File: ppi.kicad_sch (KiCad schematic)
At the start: 6 parts

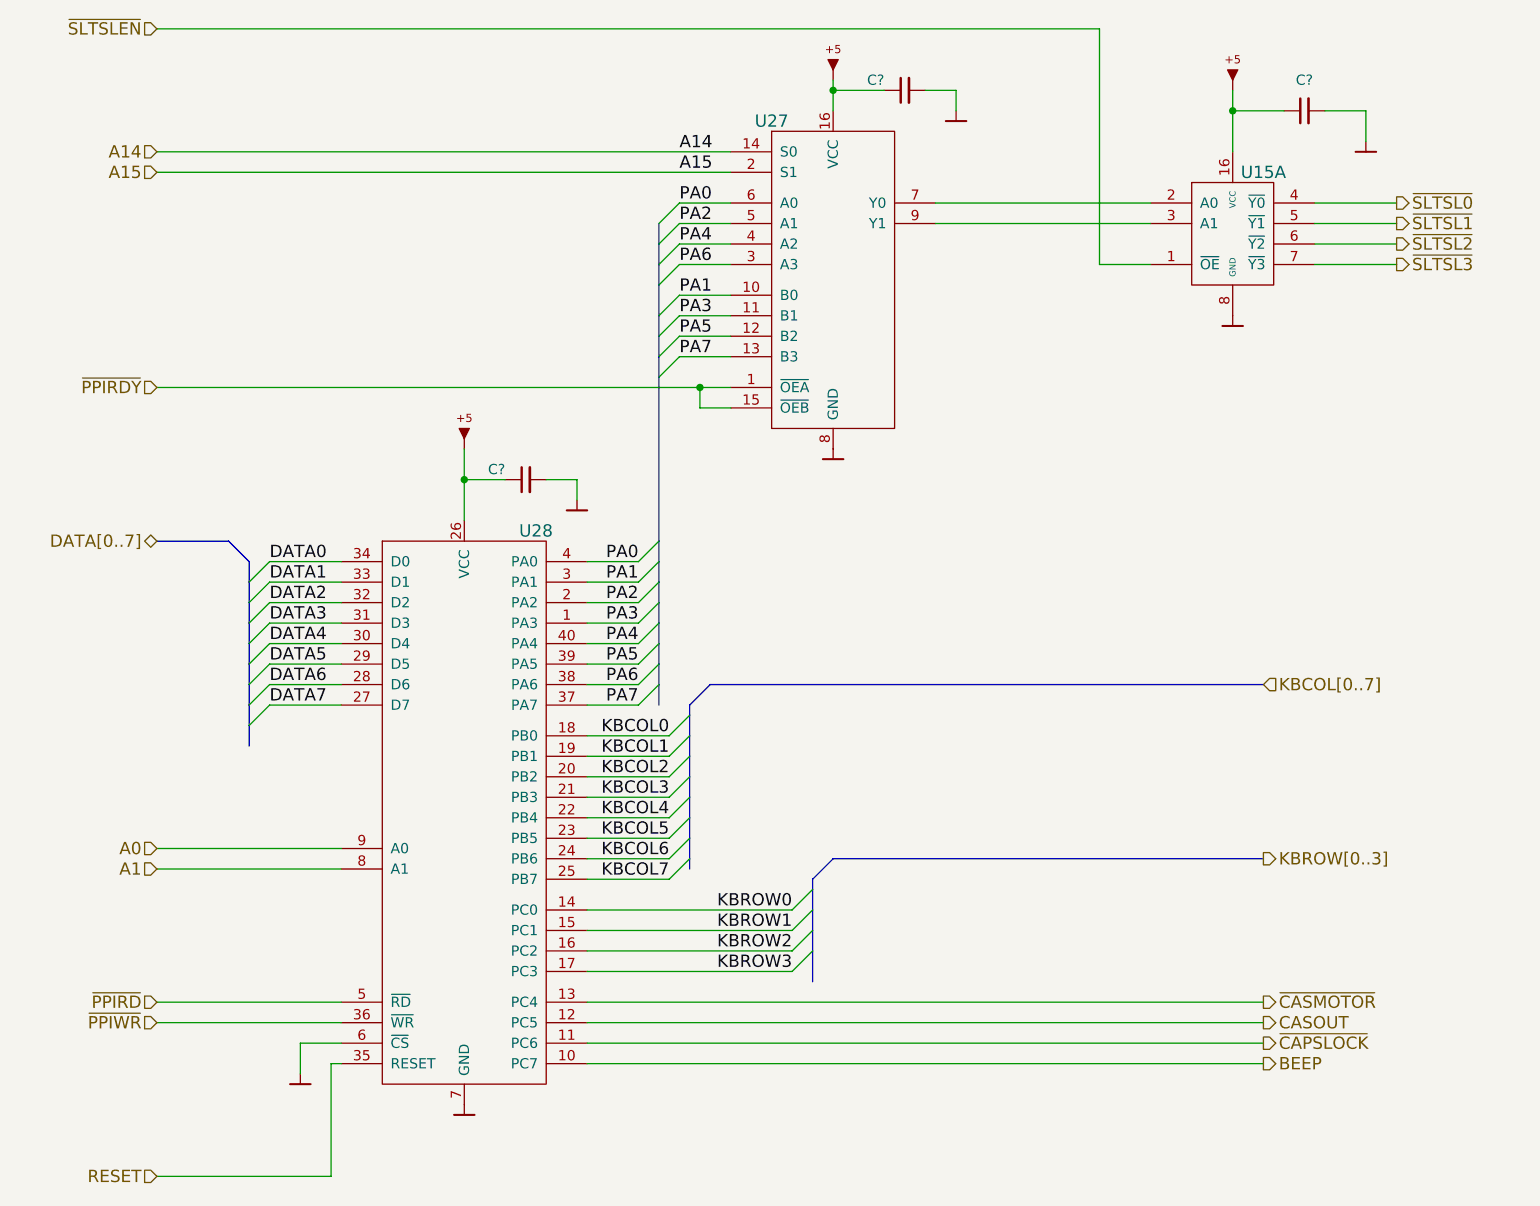
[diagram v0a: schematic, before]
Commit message: Implement power transform circuit
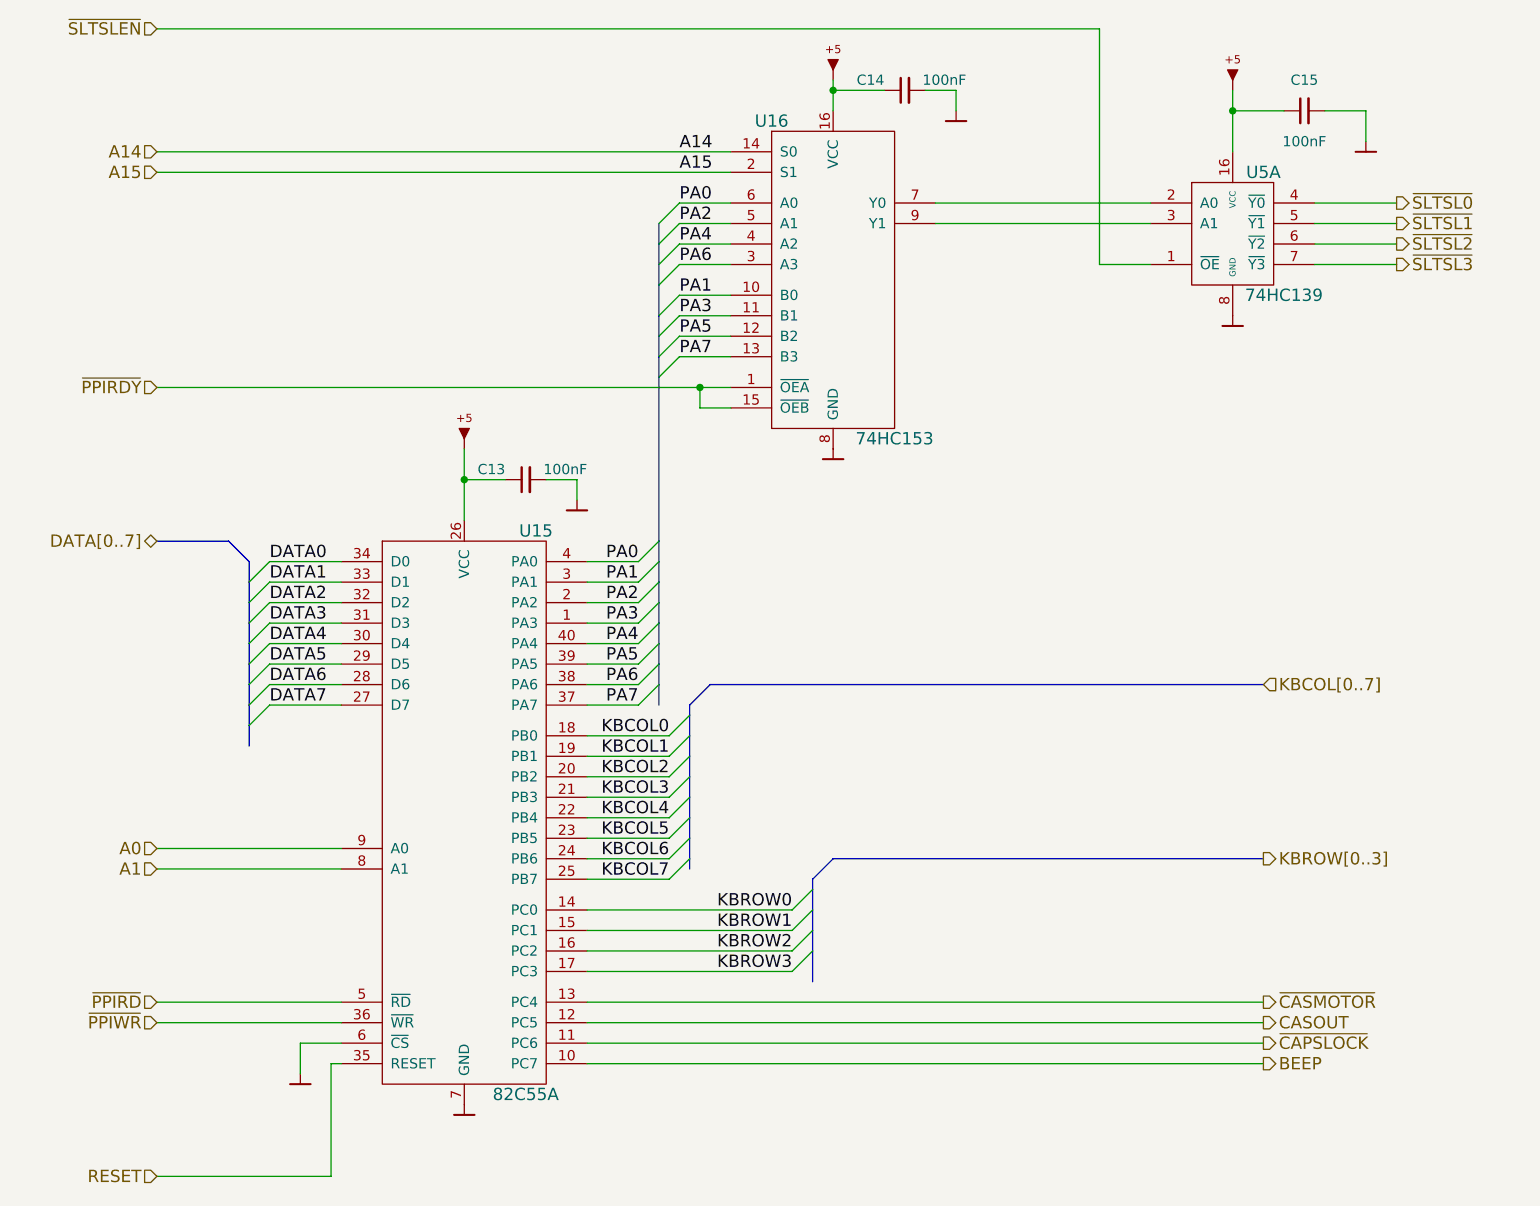
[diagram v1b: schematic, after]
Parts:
- C13, C14, C15: renamed from C?; value (none) -> 100nF; footprint (none) -> artemisa:Disc_capacitor
- U15: renamed from U28; value (none) -> 82C55A; footprint (none) -> artemisa:DIP-40_600
- U16: renamed from U27; value (none) -> 74HC153; footprint (none) -> artemisa:DIP-16_300
- U5: renamed from U15; value (none) -> 74HC139; footprint (none) -> artemisa:DIP-16_300
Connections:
- net VCC: now reaches C13.1, U15.26 (VCC)
- net VCC: now also C14.1, C15.1, U16.16 (VCC), U5.16 (VCC)
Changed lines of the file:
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@@
   (symbol (lib_id "artemisa:82C55A") (at 114.3 127 0) (unit 1)
     (in_bom yes) (on_board yes)
-    (property "Reference" "U28" (id 0) (at 123.19 90.17 0)
-      (effects (font (size 1.524 1.524)))
-    )
-    (property "Value" "" (id 1) (at 121.92 160.02 0)
-      (effects (font (size 1.524 1.524)))
-    )
-    (property "Footprint" "" (id 2) (at 119.38 113.03 0)
+    (property "Reference" "U15" (id 0) (at 123.19 90.17 0)
+      (effects (font (size 1.524 1.524)))
+    )
+    (property "Value" "82C55A" (id 1) (at 121.92 160.02 0)
+      (effects (font (size 1.524 1.524)))
+    )
+    (property "Footprint" "artemisa:DIP-40_600" (id 2) (at 119.38 113.03 0)
       (effects (font (size 1.524 1.524)) hide)
     )
@@
   (symbol (lib_id "artemisa:74HC153") (at 160.02 59.69 0) (unit 1)
     (in_bom yes) (on_board yes)
-    (property "Reference" "U27" (id 0) (at 152.4 39.37 0)
-      (effects (font (size 1.524 1.524)))
-    )
-    (property "Value" "" (id 1) (at 167.64 78.74 0)
-      (effects (font (size 1.524 1.524)))
-    )
-    (property "Footprint" "" (id 2) (at 160.02 63.5 0)
+    (property "Reference" "U16" (id 0) (at 152.4 39.37 0)
+      (effects (font (size 1.524 1.524)))
+    )
+    (property "Value" "74HC153" (id 1) (at 167.64 78.74 0)
+      (effects (font (size 1.524 1.524)))
+    )
+    (property "Footprint" "artemisa:DIP-16_300" (id 2) (at 160.02 63.5 0)
       (effects (font (size 1.524 1.524)) hide)
     )
@@
   (symbol (lib_id "artemisa:74HC139") (at 209.55 53.34 0) (unit 1)
     (in_bom yes) (on_board yes)
-    (property "Reference" "U15" (id 0) (at 213.36 45.72 0)
-      (effects (font (size 1.524 1.524)))
-    )
-    (property "Value" "" (id 1) (at 215.9 60.96 0)
-      (effects (font (size 1.524 1.524)))
-    )
-    (property "Footprint" "" (id 2) (at 209.55 57.15 0)
+    (property "Reference" "U5" (id 0) (at 213.36 45.72 0)
+      (effects (font (size 1.524 1.524)))
+    )
+    (property "Value" "74HC139" (id 1) (at 215.9 60.96 0)
+      (effects (font (size 1.524 1.524)))
+    )
+    (property "Footprint" "artemisa:DIP-16_300" (id 2) (at 209.55 57.15 0)
       (effects (font (size 1.524 1.524)) hide)
     )
@@
   (symbol (lib_id "artemisa:GND") (at 160.02 80.01 0) (unit 1)
     (in_bom yes) (on_board yes)
-    (property "Reference" "#PWR0138" (id 0) (at 160.02 82.55 0)
-      (effects (font (size 1.524 1.524)) hide)
-    )
-    (property "Value" "" (id 1) (at 160.02 77.47 0)
+    (property "Reference" "#PWR049" (id 0) (at 160.02 82.55 0)
+      (effects (font (size 1.524 1.524)) hide)
+    )
+    (property "Value" "GND" (id 1) (at 160.02 77.47 0)
       (effects (font (size 1.524 1.524)) hide)
     )
@@
   (symbol (lib_id "artemisa:VCC") (at 160.02 34.29 0) (unit 1)
     (in_bom yes) (on_board yes)
-    (property "Reference" "#PWR0135" (id 0) (at 160.02 35.56 0)
-      (effects (font (size 1.524 1.524)) hide)
-    )
-    (property "Value" "" (id 1) (at 160.02 27.94 0)
+    (property "Reference" "#PWR048" (id 0) (at 160.02 35.56 0)
+      (effects (font (size 1.524 1.524)) hide)
+    )
+    (property "Value" "VCC" (id 1) (at 160.02 27.94 0)
       (effects (font (size 1.524 1.524)) hide)
     )
@@
       (effects (font (size 1.524 1.524)) hide)
     )
-    (pin "~")
+    (pin "1")
   )
   (symbol (lib_id "artemisa:Cap") (at 168.91 35.56 90) (unit 1)
     (in_bom yes) (on_board yes)
-    (property "Reference" "C?" (id 0) (at 166.37 34.29 90)
+    (property "Reference" "C14" (id 0) (at 166.37 34.29 90)
       (effects (font (size 1.27 1.27)) (justify left))
     )
-    (property "Value" "" (id 1) (at 176.53 34.29 90)
+    (property "Value" "100nF" (id 1) (at 176.53 34.29 90)
       (effects (font (size 1.27 1.27)) (justify left))
     )
-    (property "Footprint" "" (id 2) (at 168.91 35.56 0)
+    (property "Footprint" "artemisa:Disc_capacitor" (id 2) (at 168.91 35.56 0)
       (effects (font (size 1.27 1.27)) hide)
     )
@@
   (symbol (lib_id "artemisa:GND") (at 175.26 38.1 0) (unit 1)
     (in_bom yes) (on_board yes)
-    (property "Reference" "#PWR0136" (id 0) (at 175.26 40.64 0)
-      (effects (font (size 1.524 1.524)) hide)
-    )
-    (property "Value" "" (id 1) (at 175.26 35.56 0)
+    (property "Reference" "#PWR050" (id 0) (at 175.26 40.64 0)
+      (effects (font (size 1.524 1.524)) hide)
+    )
+    (property "Value" "GND" (id 1) (at 175.26 35.56 0)
       (effects (font (size 1.524 1.524)) hide)
     )
@@
   (symbol (lib_id "artemisa:GND") (at 93.98 157.48 0) (unit 1)
     (in_bom yes) (on_board yes)
-    (property "Reference" "#PWR0140" (id 0) (at 93.98 160.02 0)
-      (effects (font (size 1.524 1.524)) hide)
-    )
-    (property "Value" "" (id 1) (at 93.98 154.94 0)
+    (property "Reference" "#PWR044" (id 0) (at 93.98 160.02 0)
+      (effects (font (size 1.524 1.524)) hide)
+    )
+    (property "Value" "GND" (id 1) (at 93.98 154.94 0)
       (effects (font (size 1.524 1.524)) hide)
     )
@@
   (symbol (lib_id "artemisa:GND") (at 114.3 161.29 0) (unit 1)
     (in_bom yes) (on_board yes)
-    (property "Reference" "#PWR0141" (id 0) (at 114.3 163.83 0)
-      (effects (font (size 1.524 1.524)) hide)
-    )
-    (property "Value" "" (id 1) (at 114.3 158.75 0)
+    (property "Reference" "#PWR046" (id 0) (at 114.3 163.83 0)
+      (effects (font (size 1.524 1.524)) hide)
+    )
+    (property "Value" "GND" (id 1) (at 114.3 158.75 0)
       (effects (font (size 1.524 1.524)) hide)
     )
@@
   (symbol (lib_id "artemisa:VCC") (at 114.3 80.01 0) (unit 1)
     (in_bom yes) (on_board yes)
-    (property "Reference" "#PWR0137" (id 0) (at 114.3 81.28 0)
-      (effects (font (size 1.524 1.524)) hide)
-    )
-    (property "Value" "" (id 1) (at 114.3 73.66 0)
+    (property "Reference" "#PWR045" (id 0) (at 114.3 81.28 0)
+      (effects (font (size 1.524 1.524)) hide)
+    )
+    (property "Value" "VCC" (id 1) (at 114.3 73.66 0)
       (effects (font (size 1.524 1.524)) hide)
     )
@@
       (effects (font (size 1.524 1.524)) hide)
     )
-    (pin "~")
+    (pin "1")
   )
   (symbol (lib_id "artemisa:Cap") (at 121.92 83.82 90) (unit 1)
     (in_bom yes) (on_board yes)
-    (property "Reference" "C?" (id 0) (at 119.38 82.55 90)
+    (property "Reference" "C13" (id 0) (at 119.38 82.55 90)
       (effects (font (size 1.27 1.27)) (justify left))
     )
-    (property "Value" "" (id 1) (at 129.54 82.55 90)
+    (property "Value" "100nF" (id 1) (at 129.54 82.55 90)
       (effects (font (size 1.27 1.27)) (justify left))
     )
-    (property "Footprint" "" (id 2) (at 121.92 83.82 0)
+    (property "Footprint" "artemisa:Disc_capacitor" (id 2) (at 121.92 83.82 0)
       (effects (font (size 1.27 1.27)) hide)
     )
@@
   (symbol (lib_id "artemisa:GND") (at 128.27 86.36 0) (unit 1)
     (in_bom yes) (on_board yes)
-    (property "Reference" "#PWR0139" (id 0) (at 128.27 88.9 0)
-      (effects (font (size 1.524 1.524)) hide)
-    )
-    (property "Value" "" (id 1) (at 128.27 83.82 0)
+    (property "Reference" "#PWR047" (id 0) (at 128.27 88.9 0)
+      (effects (font (size 1.524 1.524)) hide)
+    )
+    (property "Value" "GND" (id 1) (at 128.27 83.82 0)
       (effects (font (size 1.524 1.524)) hide)
     )
@@
   (symbol (lib_id "artemisa:GND") (at 209.55 63.5 0) (unit 1)
     (in_bom yes) (on_board yes)
-    (property "Reference" "#PWR?" (id 0) (at 209.55 66.04 0)
-      (effects (font (size 1.524 1.524)) hide)
-    )
-    (property "Value" "" (id 1) (at 209.55 60.96 0)
+    (property "Reference" "#PWR052" (id 0) (at 209.55 66.04 0)
+      (effects (font (size 1.524 1.524)) hide)
+    )
+    (property "Value" "GND" (id 1) (at 209.55 60.96 0)
       (effects (font (size 1.524 1.524)) hide)
     )
@@
   (symbol (lib_id "artemisa:VCC") (at 209.55 35.56 0) (unit 1)
     (in_bom yes) (on_board yes)
-    (property "Reference" "#PWR?" (id 0) (at 209.55 36.83 0)
-      (effects (font (size 1.524 1.524)) hide)
-    )
-    (property "Value" "" (id 1) (at 209.55 29.21 0)
+    (property "Reference" "#PWR051" (id 0) (at 209.55 36.83 0)
+      (effects (font (size 1.524 1.524)) hide)
+    )
+    (property "Value" "VCC" (id 1) (at 209.55 29.21 0)
       (effects (font (size 1.524 1.524)) hide)
     )
@@
       (effects (font (size 1.524 1.524)) hide)
     )
-    (pin "~")
+    (pin "1")
   )
   (symbol (lib_id "artemisa:Cap") (at 218.44 38.1 90) (unit 1)
     (in_bom yes) (on_board yes)
-    (property "Reference" "C?" (id 0) (at 218.44 34.29 90))
-    (property "Value" "" (id 1) (at 218.44 41.91 90))
-    (property "Footprint" "" (id 2) (at 218.44 38.1 0)
+    (property "Reference" "C15" (id 0) (at 218.44 34.29 90))
+    (property "Value" "100nF" (id 1) (at 218.44 41.91 90))
+    (property "Footprint" "artemisa:Disc_capacitor" (id 2) (at 218.44 38.1 0)
       (effects (font (size 1.27 1.27)) hide)
     )
@@
   (symbol (lib_id "artemisa:GND") (at 226.06 41.91 0) (unit 1)
     (in_bom yes) (on_board yes)
-    (property "Reference" "#PWR?" (id 0) (at 226.06 44.45 0)
-      (effects (font (size 1.524 1.524)) hide)
-    )
-    (property "Value" "" (id 1) (at 226.06 39.37 0)
-      (effects (font (size 1.524 1.524)) hide)
-    )
+    (property "Reference" "#PWR053" (id 0) (at 226.06 44.45 0)
+      (effects (font (size 1.524 1.524)) hide)
+    )
+    (property "Value" "GND" (id 1) (at 226.06 39.37 0)
+      (effects (font (size 1.524 1.524)) hide)
+    )
